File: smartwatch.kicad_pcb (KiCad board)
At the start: 2 copper layers, 40 x 40 mm, 44 parts, among them IC1 LTC4413EDD-1#PBF, IC2 NORA-B120-00B, J1 Conn_01x01_Pin, J2 Conn_01x01_Pin, J3 5022441530, J5 Conn_01x06_Pin, Q1 2N7002-7-F, U1 MAX17048G+T10, U10 AP2127K-1.8, U2 AP2112K-3.3TRG1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

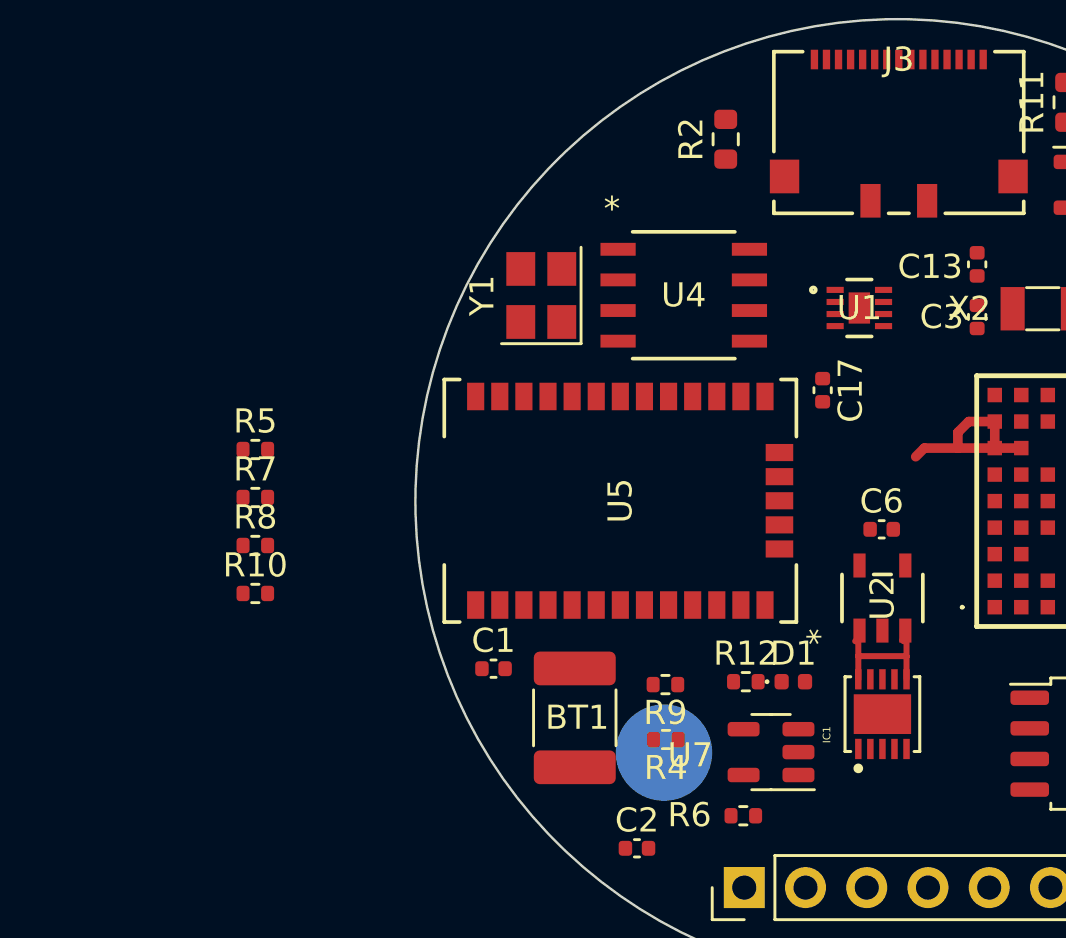
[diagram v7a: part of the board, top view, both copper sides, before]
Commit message: added battery gauge
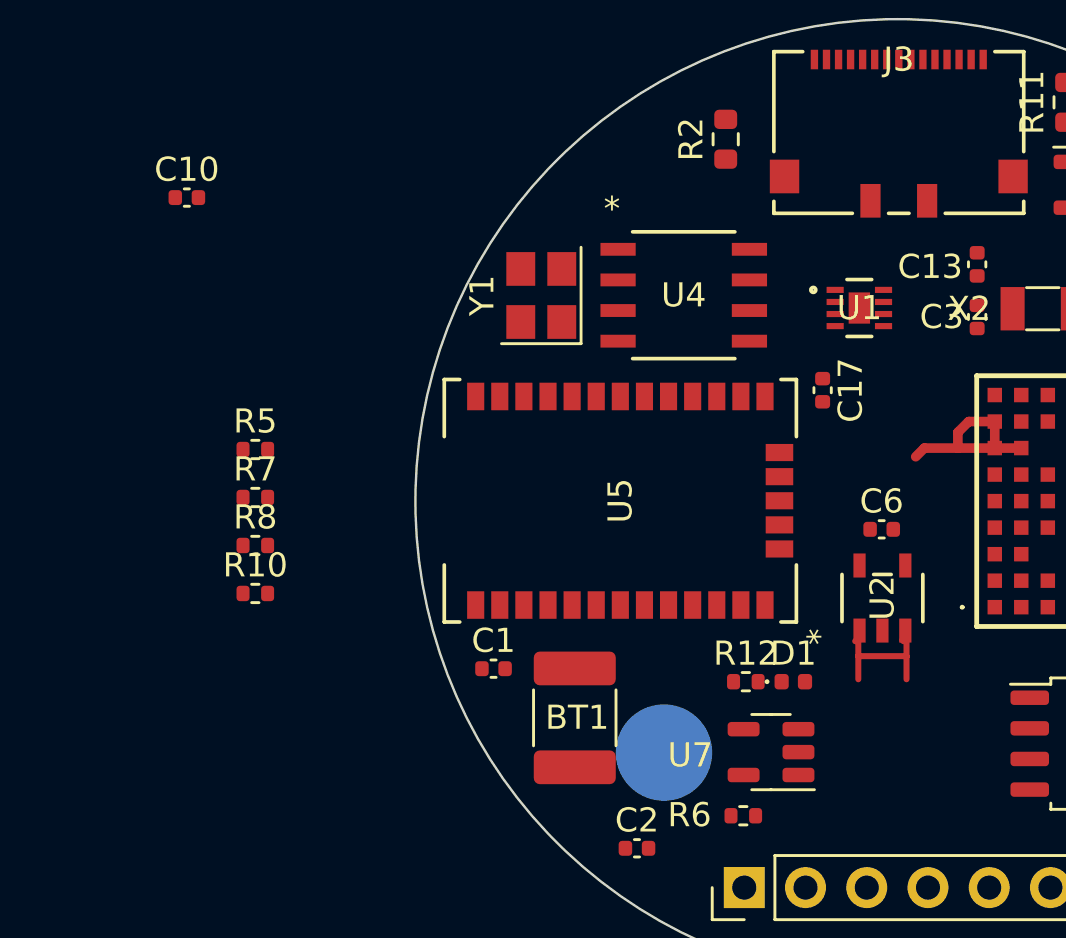
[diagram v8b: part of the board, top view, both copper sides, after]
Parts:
- removed IC1: LTC4413EDD-1#PBF, LTC4413EDD_PBF:SON50P300X300X80-11N
- removed R4: 800k, Resistor_SMD:R_0402_1005Metric
- removed R9: 2M, Resistor_SMD:R_0402_1005Metric
- added C10: 100uF, Capacitor_SMD:C_0402_1005Metric, F.Cu at (129.5, 80.0)
- C6: value 1uF -> 100uF
- R6: value 10k -> 5.1k
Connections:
- U1 pad 1: unconnected-(U1-CTG-Pad1) -> Net-(BT1-+)
- U1 pad 2: unconnected-(U1-CELL-Pad2) -> Net-(BT1-+)
- U1 pad 3: unconnected-(U1-VDD-Pad3) -> GND
- U1 pad 4: unconnected-(U1-GND-Pad4) -> GND
- U1 pad 6: unconnected-(U1-QSTRT-Pad6) -> GND
- U1 pad 7: unconnected-(U1-SCL-Pad7) -> /GAUGE_SCL
- U1 pad 8: unconnected-(U1-SDA-Pad8) -> /GAUGE_SDA
- U1 pad 9: unconnected-(U1-EPAD-Pad9) -> GND
